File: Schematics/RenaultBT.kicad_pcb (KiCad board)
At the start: 2 copper layers, 160 x 100.3 mm, 57 parts, among them J1 PowerSupply, J2 SPDIF_Output, J3 HU_CDC_Interface, Q1 2N7000, Q2 2N7000, Q3 2N7000, Q4 2N7000, U1 LM2575-5.0BT, U2 LM1117-3.3, U3 WM8804, U4 CSRA64215, U5 74HC04, U6 STM32F103, Y1 12Mhz

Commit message: Modified PCB design
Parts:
- R5: footprint Resistor_THT:R_Axial_DIN0207_L6.3mm_D2.5mm_P10.16mm_Horizontal -> Resistor_THT:R_Axial_DIN0207_L6.3mm_D2.5mm_P7.62mm_Horizontal
- moved R26 15.3 mm to (191.8, 108.0)
- moved R24 15.3 mm to (191.8, 114.3)
- moved R25 15.3 mm to (181.6, 104.1)
- moved J3 15.2 mm to (203.2, 111.8)
- moved Q2 15.2 mm to (195.6, 113.0)
- moved Q4 15.2 mm to (195.6, 110.5)
- moved C5 2.54 mm to (177.8, 115.6)
- moved Q3 2.54 mm to (174.0, 133.3)
- moved R3 2.54 mm to (174.0, 125.7)
- moved Y1 2.54 mm to (163.8, 108.0)
- moved C6 2.54 mm to (168.9, 109.2)
- moved C7 2.54 mm to (153.7, 109.2)
- moved C8 2.54 mm to (148.6, 115.6)
- moved R4 2.54 mm to (171.4, 123.2)
- moved R7 2.54 mm to (151.1, 125.7)
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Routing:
- net /I2SToSPDIF/DGND: track 0.00 -> 75.0 mm
- net /HU_CDC_InterfaceAdapter/3V3: track 0.00 -> 54.9 mm
- net Net-(C9-Pad2): track 0.00 -> 32.2 mm
- net Net-(U5-Pad11): track 0.00 -> 31.1 mm
- net Net-(Q3-Pad3): track 0.00 -> 11.2 mm
- net Net-(C7-Pad1): track 0.00 -> 10.4 mm
- net /I2SToSPDIF/SPDIF_OUTPUT: track 0.00 -> 10.2 mm
- net Net-(C6-Pad1): track 0.00 -> 10.2 mm
- net /HU_CDC_InterfaceAdapter/HU_RX: track 0.00 -> 8.89 mm
- net /HU_CDC_InterfaceAdapter/HU_TX: track 0.00 -> 7.62 mm
- net Net-(R3-Pad1): track 0.00 -> 5.08 mm
- net Net-(C9-Pad1): track 0.00 -> 3.85 mm
- net Net-(Q4-Pad3): track 0.00 -> 3.81 mm
- net Net-(Q2-Pad2): track 0.00 -> 3.81 mm

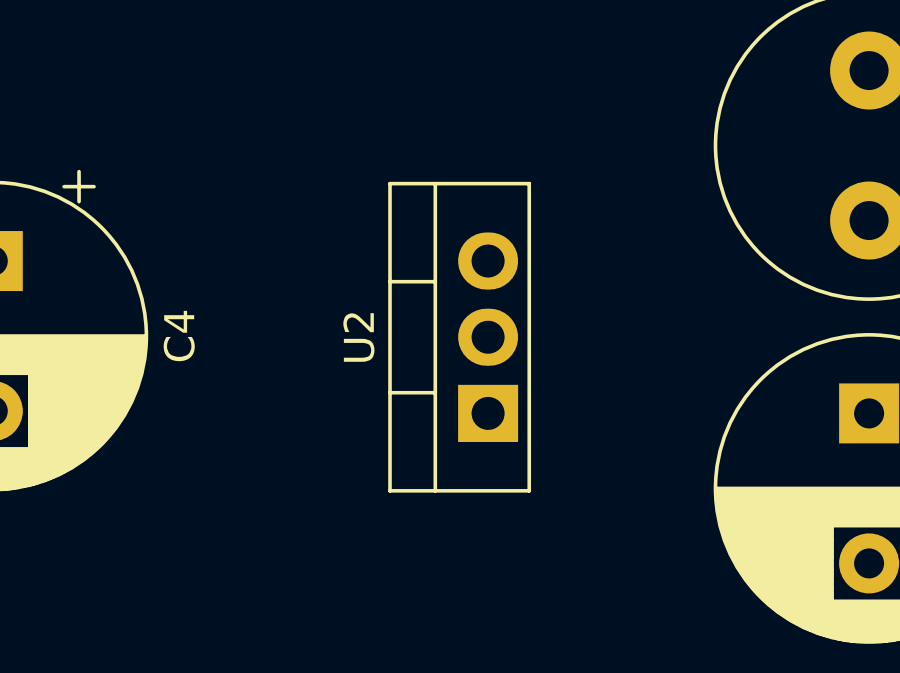
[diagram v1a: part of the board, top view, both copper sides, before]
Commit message: Modified power supply schematic and PCB design; added new library for lm3940 IC.
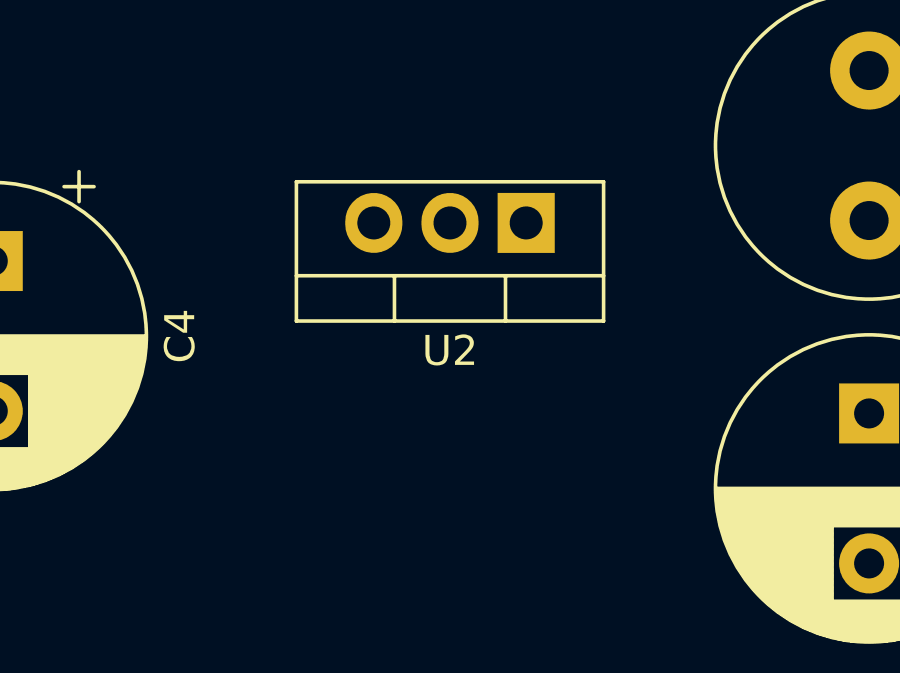
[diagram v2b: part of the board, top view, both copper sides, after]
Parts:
- U2: value LM1117-3.3 -> LM3940
- moved U2 6.48 mm to (152.4, 47.0), turned to 180 degrees
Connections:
- U2 pad 1: /I2SToSPDIF/DGND -> /PowerSupply/5V
- U2 pad 2: /HU_CDC_InterfaceAdapter/3V3 -> /I2SToSPDIF/DGND
- U2 pad 3: /PowerSupply/5V -> /HU_CDC_InterfaceAdapter/3V3

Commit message: Modified PCB design
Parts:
- C4: value 100uF -> 470uF; footprint Capacitor_THT:CP_Radial_D10.0mm_P5.00mm -> Capacitor_THT:CP_Radial_D8.0mm_P3.50mm
- moved D1 7.73 mm to (165.1, 41.9)
- moved C2 7.62 mm to (156.2, 53.3)
- moved L1 7.62 mm to (156.2, 41.9)
- moved U2 7.62 mm to (144.8, 47.0)
- moved C4 6.48 mm to (128.3, 47.0)
- moved U1 6.35 mm to (172.7, 41.9)
- moved R1 5.08 mm to (181.6, 55.9), turned to 90 degrees
- moved C8 3.81 mm to (144.8, 115.6)
- moved Q1 1.27 mm to (194.3, 54.6)
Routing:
- net /I2SToSPDIF/DGND: track 75.0 -> 318.0 mm
- net /HU_CDC_InterfaceAdapter/3V3: track 54.9 -> 164.2 mm
- net /I2SToSPDIF/SPDIFOutput_buffered/SPDIF_TTL: track 0.00 -> 49.5 mm
- net /PowerSupply/5V: track 0.00 -> 34.4 mm
- net /PowerSupply/12V: track 0.00 -> 31.5 mm
- net /PowerSupply/HU_ON: track 0.00 -> 25.7 mm
- net PWR_ON: track 0.00 -> 22.0 mm
- net Net-(D1-Pad1): track 0.00 -> 18.6 mm
- net /I2SToSPDIF/I2S_SD_IN: track 0.00 -> 17.8 mm
- net /BTModule/I2S_WS: track 0.00 -> 17.8 mm
- net /BTModule/I2S_CLK: track 0.00 -> 17.8 mm
- net Net-(JP1-Pad1): track 0.00 -> 15.2 mm
- net Net-(R20-Pad1): track 0.00 -> 9.72 mm
- net /MainController/I2C1_SCL: track 0.00 -> 7.62 mm
- net /MainController/I2S2_SCL: track 0.00 -> 3.81 mm
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
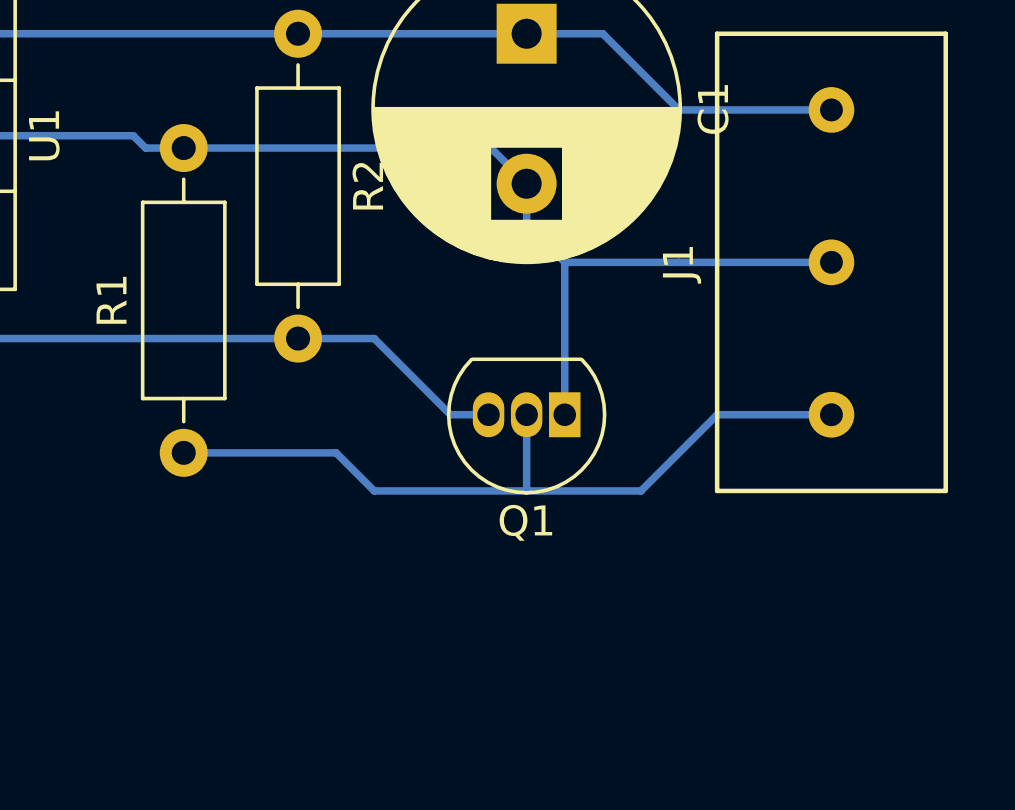
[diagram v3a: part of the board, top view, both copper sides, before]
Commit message: Updated power supply schematic and PCB design
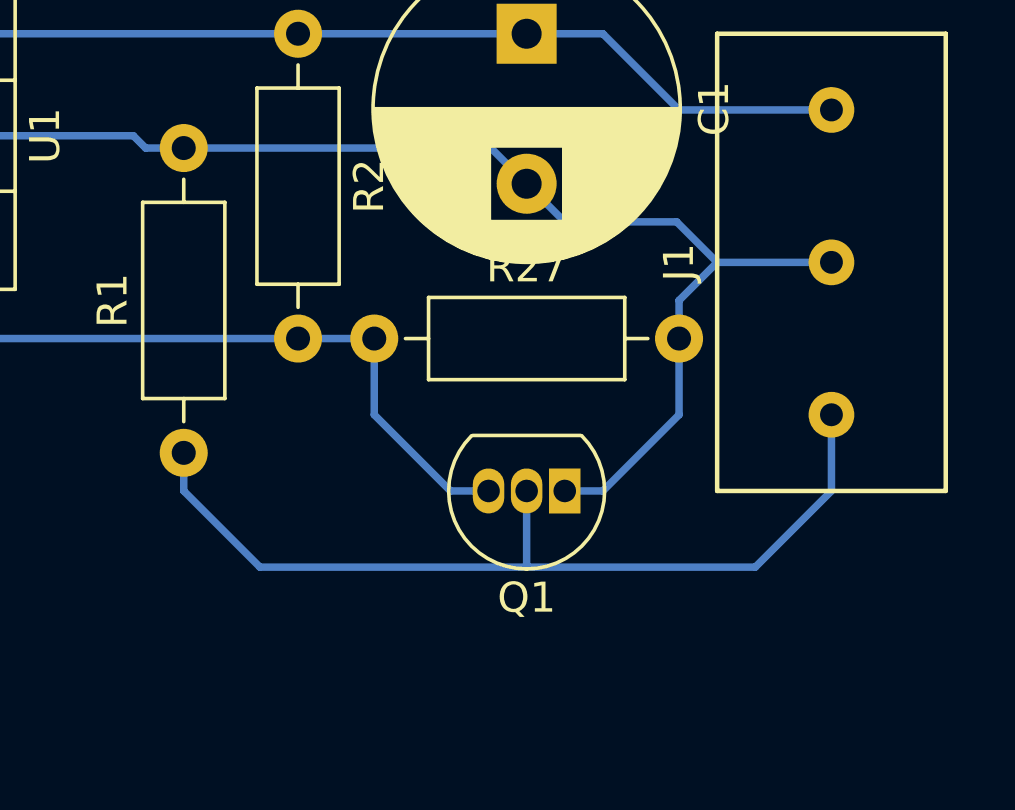
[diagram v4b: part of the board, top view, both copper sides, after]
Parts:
- added R27: 51K, Resistor_THT:R_Axial_DIN0207_L6.3mm_D2.5mm_P10.16mm_Horizontal, F.Cu at (188.0, 52.1)
- R2: value 10K -> 51K
- moved Q1 2.54 mm to (194.3, 57.1)
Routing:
- net /I2SToSPDIF/DGND: track 318.0 -> 322.6 mm
- net /PowerSupply/HU_ON: track 25.7 -> 30.0 mm
- net PWR_ON: track 22.0 -> 24.6 mm

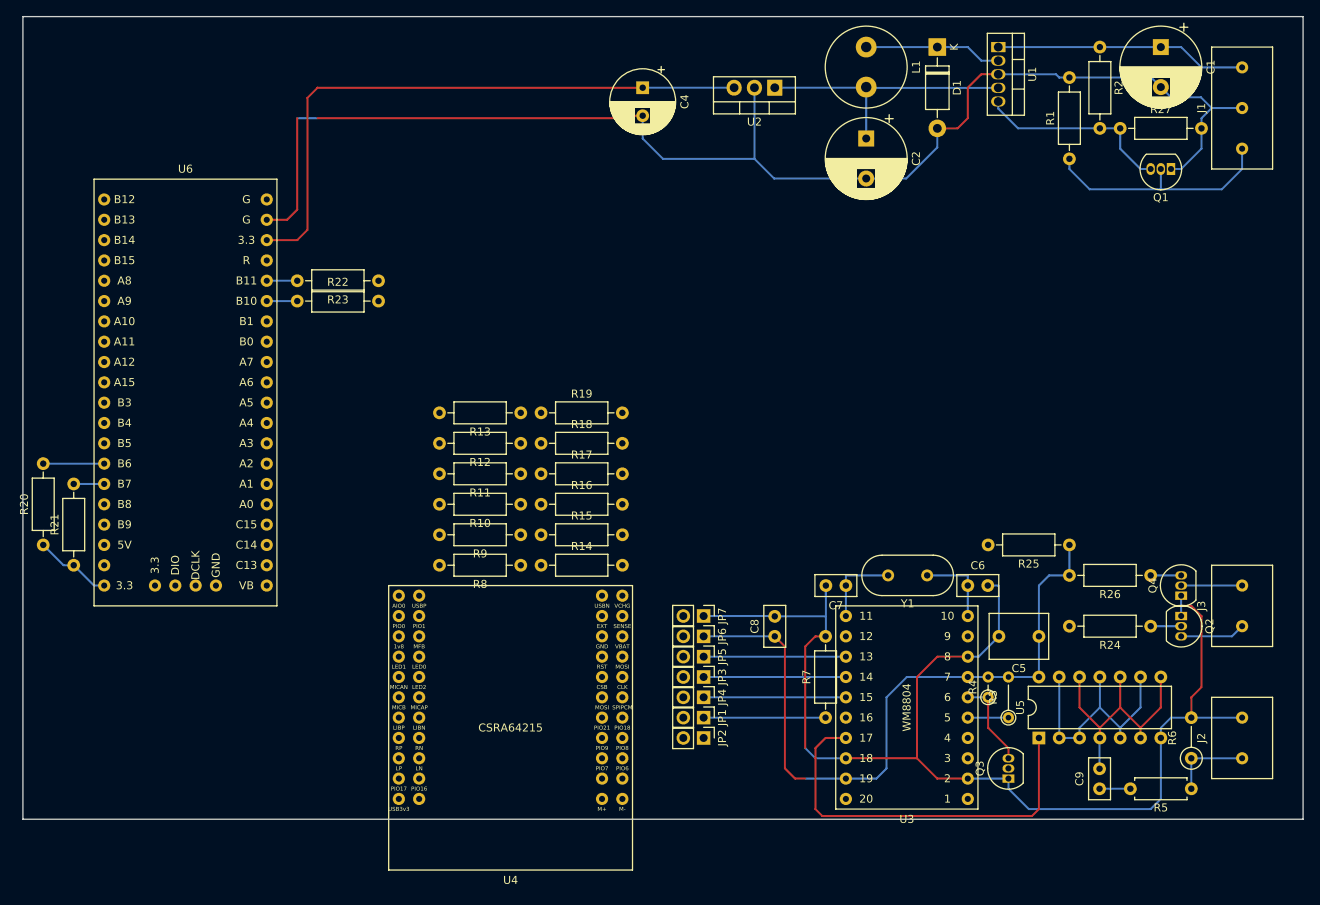
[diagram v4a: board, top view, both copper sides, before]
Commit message: Fixed CDC interface schematic; Fixed SPDIF output interface schematic; Added screw terminals; Modified PCB design
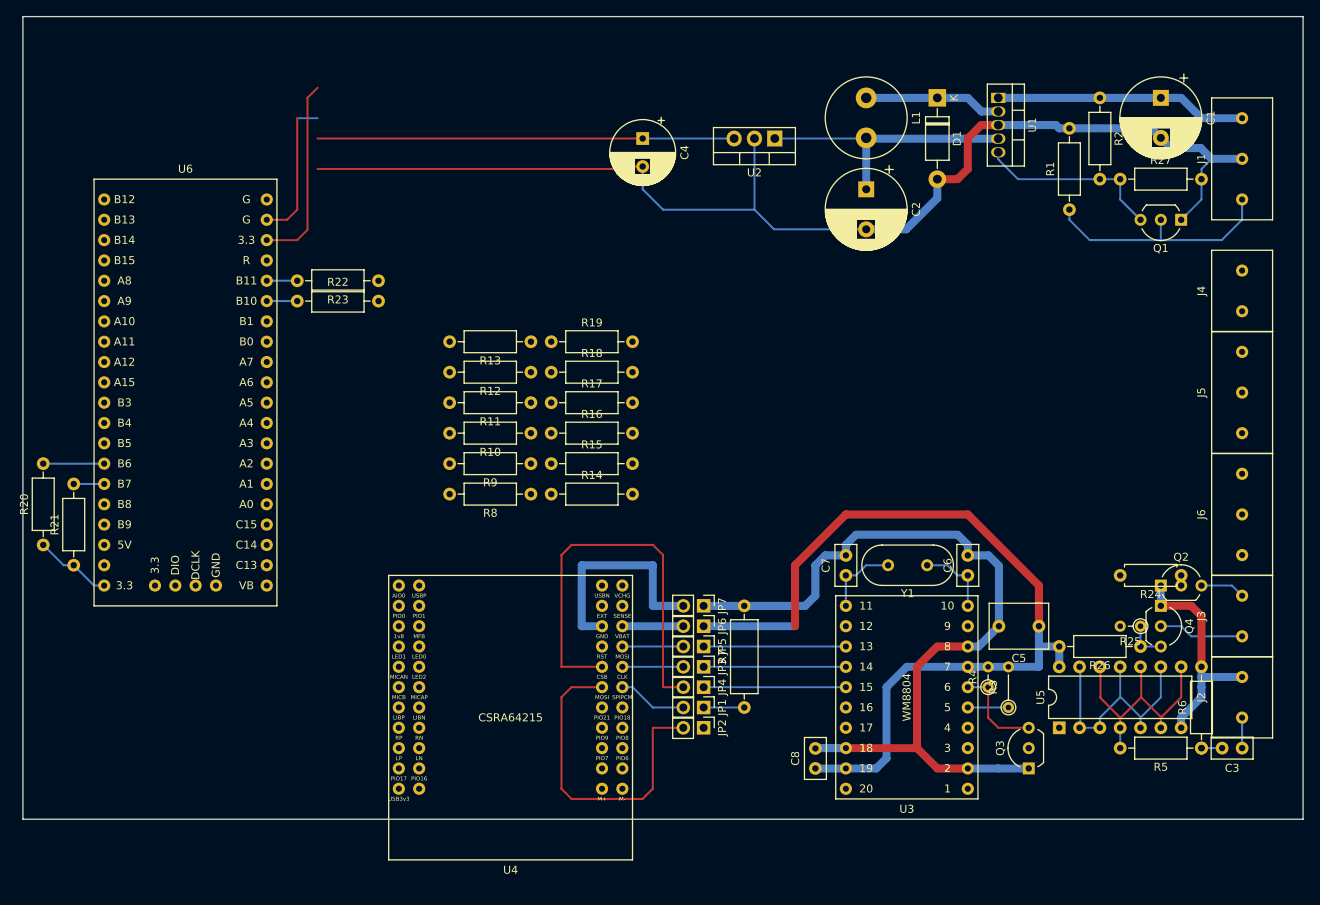
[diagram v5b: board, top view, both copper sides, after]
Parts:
- removed C9: 150n, Capacitor_THT:C_Disc_D5.0mm_W2.5mm_P2.50mm
- added C3: 0.1u, Capacitor_THT:C_Disc_D5.0mm_W2.5mm_P2.50mm, F.Cu at (203.2, 129.5)
- added J4: Screw_Terminal_01x02, ScrewTerminal:ScrewTerminal_2, F.Cu at (203.2, 72.4)
- added J5: Screw_Terminal_01x03, ScrewTerminal:ScrewTerminal_3, F.Cu at (203.2, 85.1)
- added J6: Screw_Terminal_01x03, ScrewTerminal:ScrewTerminal_3, F.Cu at (203.2, 100.3)
- Q1, Q2, Q3, Q4: footprint Package_TO_SOT_THT:TO-92_Inline -> Package_TO_SOT_THT:TO-92_Inline_Wide
- R24: footprint Resistor_THT:R_Axial_DIN0207_L6.3mm_D2.5mm_P10.16mm_Horizontal -> Resistor_THT:R_Axial_DIN0207_L6.3mm_D2.5mm_P7.62mm_Horizontal
- R25: footprint Resistor_THT:R_Axial_DIN0207_L6.3mm_D2.5mm_P10.16mm_Horizontal -> Resistor_THT:R_Axial_DIN0204_L3.6mm_D1.6mm_P2.54mm_Vertical
- R5: value 374 -> 210; footprint Resistor_THT:R_Axial_DIN0207_L6.3mm_D2.5mm_P7.62mm_Horizontal -> Resistor_THT:R_Axial_DIN0207_L6.3mm_D2.5mm_P10.16mm_Horizontal
- R6: value 93 -> 110; footprint Resistor_THT:R_Axial_DIN0207_L6.3mm_D2.5mm_P5.08mm_Vertical -> Resistor_THT:R_Axial_DIN0207_L6.3mm_D2.5mm_P10.16mm_Horizontal
- R7: footprint Resistor_THT:R_Axial_DIN0207_L6.3mm_D2.5mm_P10.16mm_Horizontal -> Resistor_THT:R_Axial_DIN0309_L9.0mm_D3.2mm_P12.70mm_Horizontal
- moved C8 17.3 mm to (149.9, 132.1)
- moved R25 13.5 mm to (190.5, 114.3)
- moved R7 10.2 mm to (141.0, 124.5)
- moved R14 8.98 mm to (116.8, 97.8)
- moved R15 8.98 mm to (116.8, 94.0)
- moved R16 8.98 mm to (116.8, 90.2)
- moved R17 8.98 mm to (116.8, 86.4)
- moved R18 8.98 mm to (116.8, 82.5)
- moved R19 8.98 mm to (116.8, 78.7)
- moved R26 8.98 mm to (190.5, 116.8)
- moved R10 8.98 mm to (114.3, 90.2)
- moved R11 8.98 mm to (114.3, 86.4)
- moved R12 8.98 mm to (114.3, 82.5)
- moved R13 8.98 mm to (114.3, 78.7)
- moved R8 8.98 mm to (114.3, 97.8)
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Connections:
- J3 pad 1: /HU_CDC_InterfaceAdapter/HU_RX -> /HU_CDC_InterfaceAdapter/HU_TX
- J3 pad 2: /HU_CDC_InterfaceAdapter/HU_TX -> /HU_CDC_InterfaceAdapter/HU_RX
- R25 pad 1: /HU_CDC_InterfaceAdapter/3V3 -> Net-(Q4-Pad3)
- R5 pad 1: /I2SToSPDIF/SPDIF_OUTPUT -> Net-(C3-Pad2)
- R5 pad 2: Net-(C9-Pad1) -> Net-(R5-Pad2)
- R6 pad 1: /I2SToSPDIF/SPDIF_OUTPUT -> Net-(C3-Pad2)
- U5 pad 10: Net-(C9-Pad2) -> Net-(R5-Pad2)
- U5 pad 12: Net-(C9-Pad2) -> Net-(R5-Pad2)
- U5 pad 4: Net-(C9-Pad2) -> Net-(R5-Pad2)
- U5 pad 6: Net-(C9-Pad2) -> Net-(R5-Pad2)
- U5 pad 8: Net-(C9-Pad2) -> Net-(R5-Pad2)
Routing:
- net Net-(JP4-Pad2): track 0.00 -> 51.9 mm
- net /I2SToSPDIF/SPDIFOutput_buffered/SPDIF_TTL: track 49.5 -> 0.00 mm
- net Net-(JP2-Pad2): track 0.00 -> 40.9 mm
- net Net-(C9-Pad2): track 32.2 -> 0.00 mm
- net Net-(R5-Pad2): track 0.00 -> 30.9 mm
- net Net-(JP7-Pad2): track 0.00 -> 27.9 mm
- net /I2SToSPDIF/DGND: track 322.6 -> 297.4 mm
- net /HU_CDC_InterfaceAdapter/3V3: track 164.2 -> 185.5 mm
- net Net-(JP1-Pad1): track 15.2 -> 5.08 mm
- net Net-(JP1-Pad2): track 0.00 -> 8.67 mm
- net Net-(JP6-Pad2): track 0.00 -> 7.62 mm
- net Net-(JP5-Pad2): track 0.00 -> 7.62 mm
- net Net-(JP3-Pad2): track 0.00 -> 7.62 mm
- net /I2SToSPDIF/SPDIF_OUTPUT: track 10.2 -> 3.81 mm
- net Net-(C9-Pad1): track 3.85 -> 0.00 mm
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
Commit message: Added C9 bypass capacitor; minor PCB design fixes
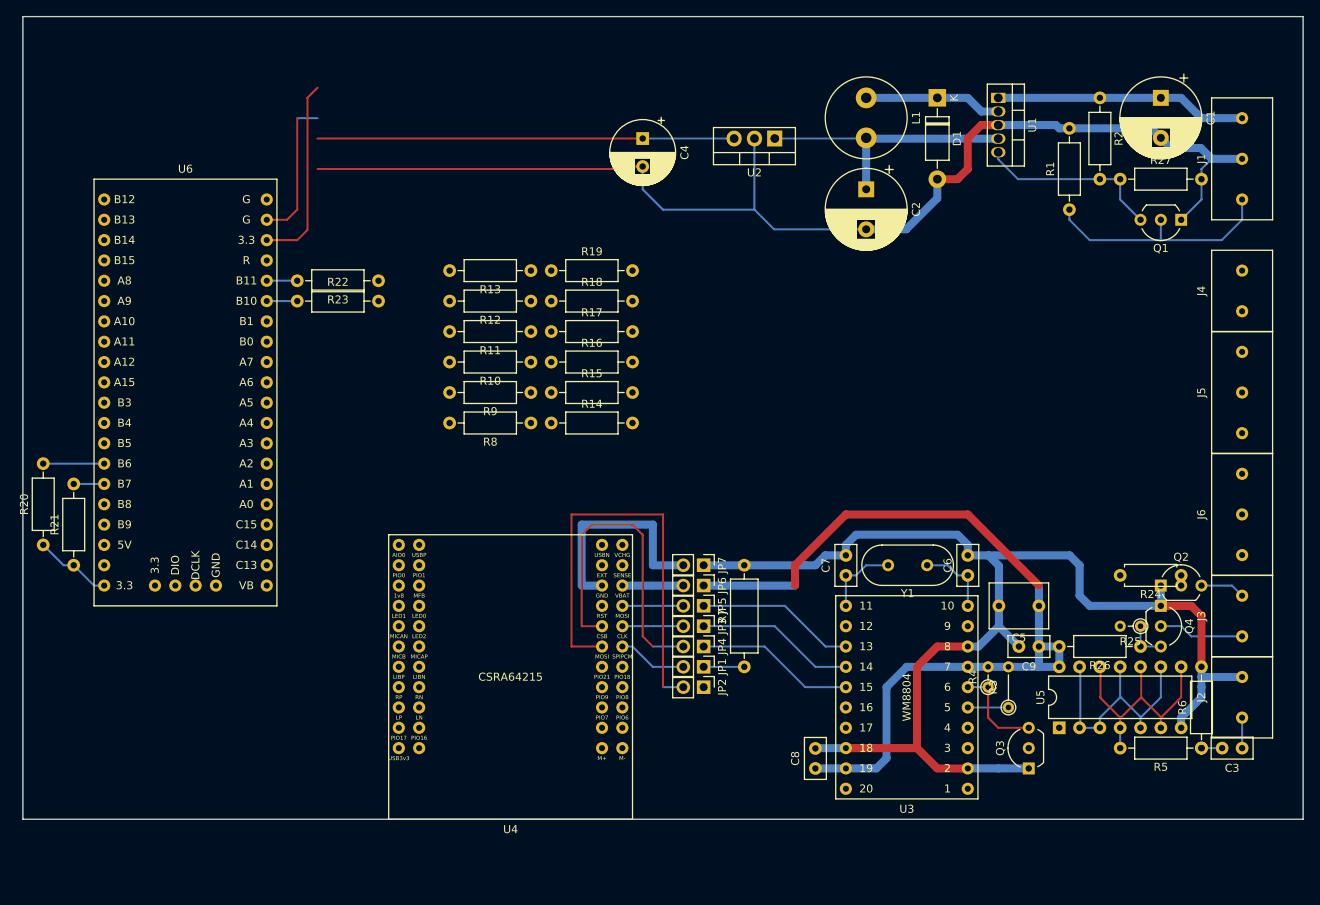
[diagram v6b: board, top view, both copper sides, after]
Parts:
- added C9: 0.1uF, Capacitor_THT:C_Disc_D5.0mm_W2.5mm_P2.50mm, F.Cu at (177.8, 116.8)
- moved R10 8.89 mm to (114.3, 81.3)
- moved R11 8.89 mm to (114.3, 77.5)
- moved R12 8.89 mm to (114.3, 73.7)
- moved R13 8.89 mm to (114.3, 69.8)
- moved R14 8.89 mm to (116.8, 88.9)
- moved R15 8.89 mm to (116.8, 85.1)
- moved R16 8.89 mm to (116.8, 81.3)
- moved R17 8.89 mm to (116.8, 77.5)
- moved R18 8.89 mm to (116.8, 73.7)
- moved R19 8.89 mm to (116.8, 69.8)
- moved R8 8.89 mm to (114.3, 88.9)
- moved R9 8.89 mm to (114.3, 85.1)
- moved JP1 5.08 mm to (135.9, 119.4)
- moved JP2 5.08 mm to (135.9, 121.9)
- moved JP3 5.08 mm to (135.9, 114.3)
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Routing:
- net /I2SToSPDIF/DGND: track 297.4 -> 323.0 mm
- net Net-(JP2-Pad2): track 40.9 -> 55.9 mm
- net Net-(JP4-Pad2): track 51.9 -> 40.9 mm
- net /HU_CDC_InterfaceAdapter/3V3: track 185.5 -> 182.9 mm
- net /I2SToSPDIF/I2S_SD_IN: track 17.8 -> 19.9 mm
- net /BTModule/I2S_WS: track 17.8 -> 19.9 mm
- net /BTModule/I2S_CLK: track 17.8 -> 19.9 mm

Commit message: Minor PCB design fixes
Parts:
- R6: footprint Resistor_THT:R_Axial_DIN0207_L6.3mm_D2.5mm_P10.16mm_Horizontal -> Resistor_THT:R_Axial_DIN0309_L9.0mm_D3.2mm_P12.70mm_Horizontal
- moved C3 5.08 mm to (203.2, 134.6)
- moved R5 5.08 mm to (198.1, 134.6)
- moved R6 5.08 mm to (198.1, 134.6)
- moved U5 5.08 mm to (180.3, 132.1)
- moved C5 3.81 mm to (174.0, 111.8)
- moved C6 3.81 mm to (165.1, 108.0)
- moved C8 3.81 mm to (146.1, 132.1)
- moved Q3 3.81 mm to (172.7, 132.1)
- moved R3 3.81 mm to (170.2, 124.5)
- moved R4 3.81 mm to (167.6, 121.9)
- moved U3 3.81 mm to (157.5, 123.2)
- moved Y1 3.81 mm to (160.0, 106.7)
- moved C7 3.81 mm to (149.9, 108.0)
- moved Q2 2.54 mm to (193.0, 111.8)
- moved R25 2.54 mm to (190.5, 116.8)
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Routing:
- net /I2SToSPDIF/DGND: track 323.0 -> 315.2 mm
- net /I2SToSPDIF/SPDIF_OUTPUT: track 3.81 -> 8.89 mm
- net /HU_CDC_InterfaceAdapter/3V3: track 182.9 -> 178.2 mm
- net /I2SToSPDIF/I2S_SD_IN: track 19.9 -> 16.5 mm
- net /BTModule/I2S_WS: track 19.9 -> 16.5 mm
- net /BTModule/I2S_CLK: track 19.9 -> 16.5 mm
- net /HU_CDC_InterfaceAdapter/HU_TX: track 10.7 -> 8.89 mm
- net /HU_CDC_InterfaceAdapter/HU_RX: track 5.61 -> 5.08 mm
